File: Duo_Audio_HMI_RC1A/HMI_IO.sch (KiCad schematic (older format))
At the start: 57 parts, among them P1 CONN_2_SMD_BACKLIGHT, P2 CONN_2_SMD_BACKLIGHT, P3 HEADER_4X1

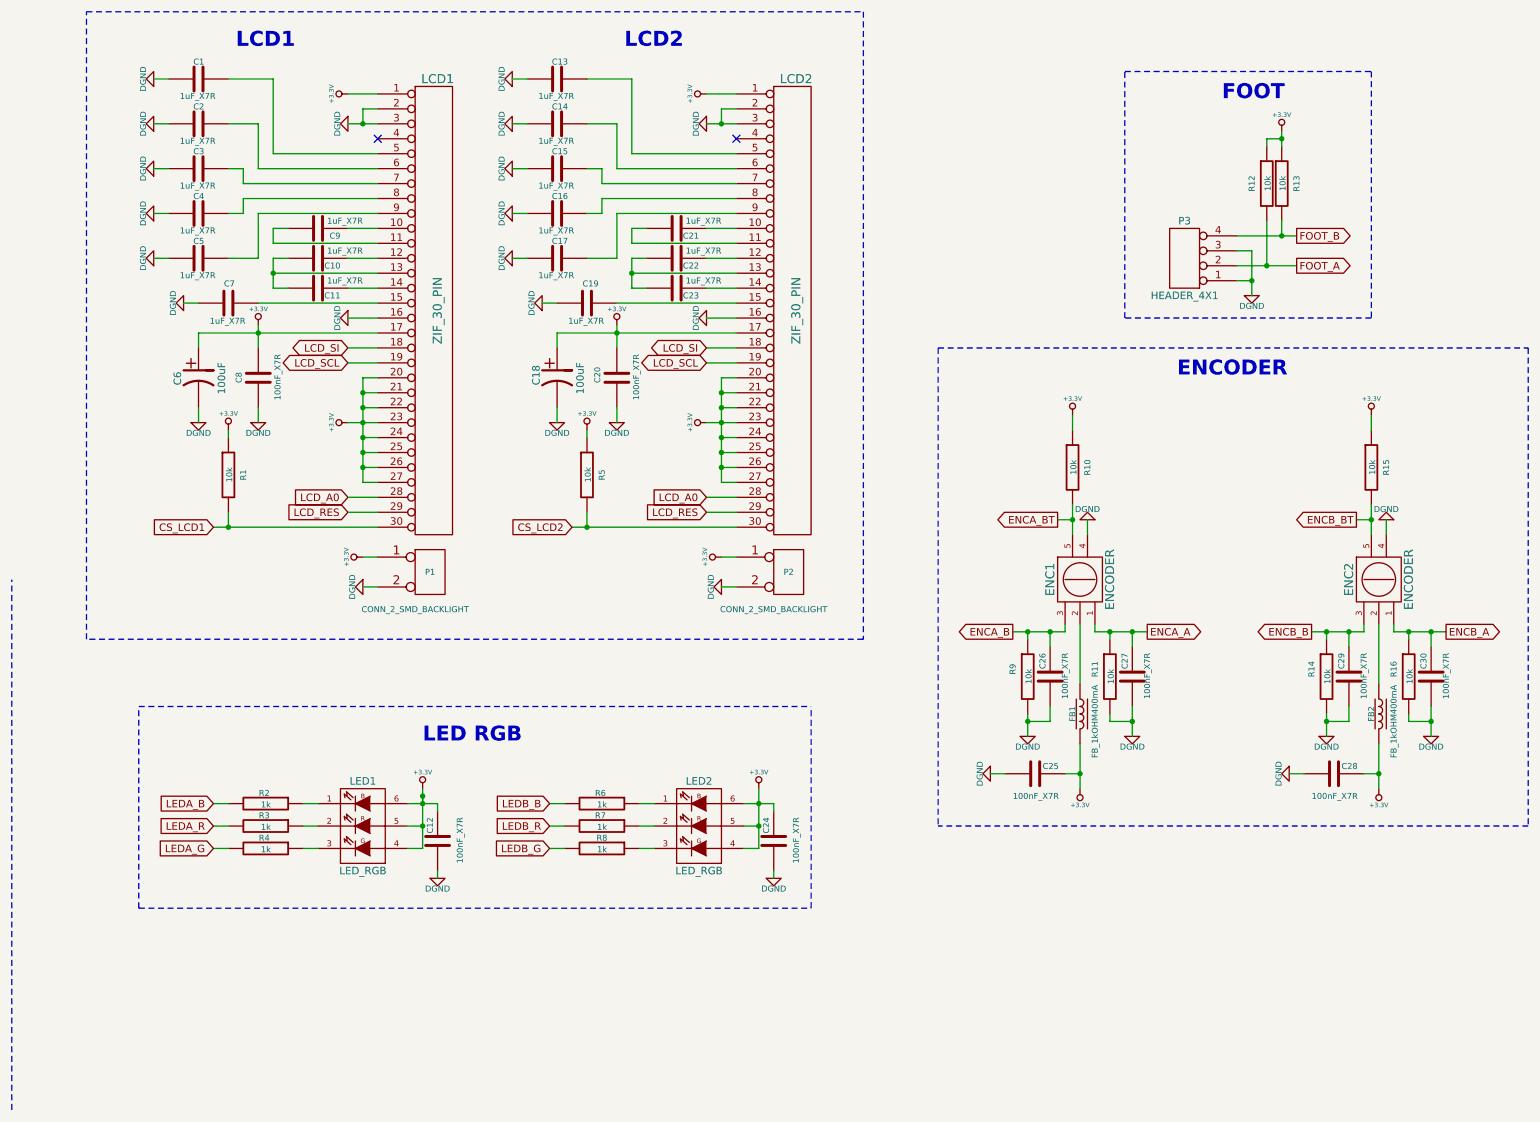
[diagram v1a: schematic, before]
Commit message: Major changes on hardware architecture. Migrating to a HMI separated board. HMI schematic finalized.
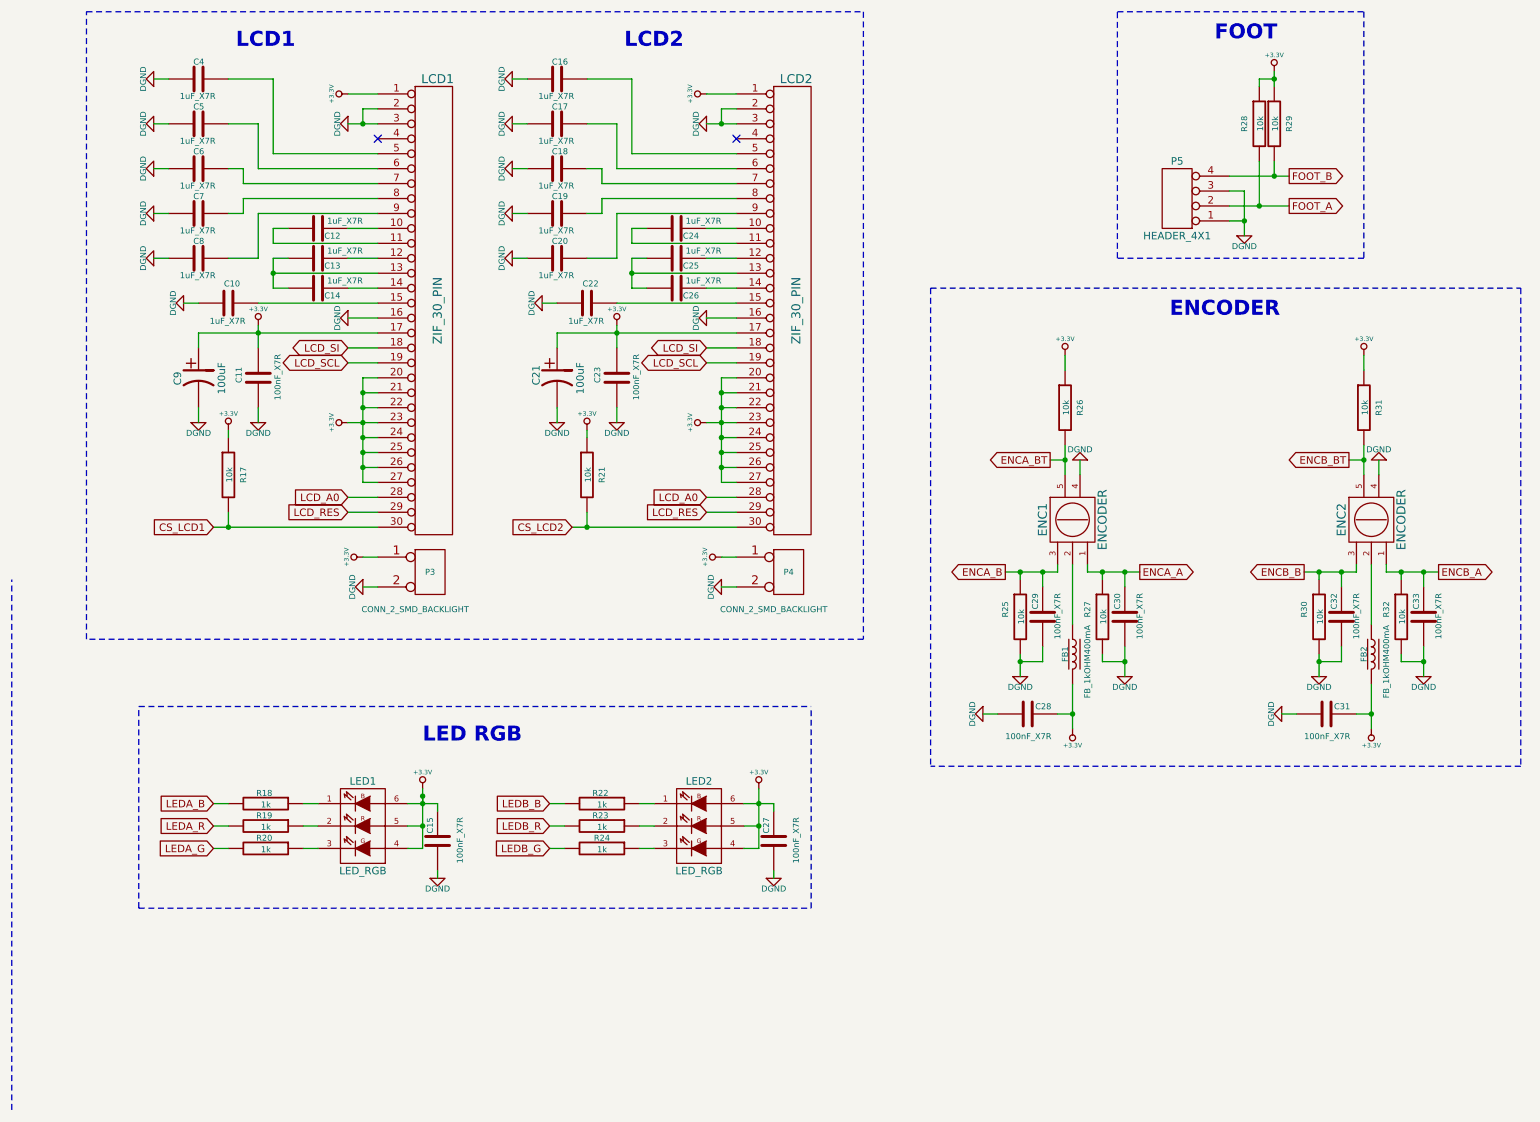
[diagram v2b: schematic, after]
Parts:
- renumbered C7 to C10, C8 to C11, C9 to C12, C10 to C13, C11 to C14, C12 to C15, C13 to C16, C14 to C17, C15 to C18, C16 to C19, C17 to C20, C18 to C21, C19 to C22, C20 to C23, C21 to C24, C22 to C25, C23 to C26, C24 to C27, C25 to C28, C26 to C29, C27 to C30, C28 to C31, C29 to C32, C30 to C33, C1 to C4, C2 to C5, C3 to C6, C4 to C7, C5 to C8, C6 to C9, P1 to P3, P2 to P4, P3 to P5, R1 to R17, R2 to R18, R3 to R19, R4 to R20, R5 to R21, R6 to R22, R7 to R23, R8 to R24, R9 to R25, R10 to R26, R11 to R27, R12 to R28, R13 to R29, R14 to R30, R15 to R31, R16 to R32
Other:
- moved on the sheet: C28, C29, C30, C31, C32, C33, ENC1, ENC2, FB1, FB2, P5, R25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
